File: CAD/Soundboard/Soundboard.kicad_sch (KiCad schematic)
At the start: 23 parts, among them P1 USB_C_Plug_USB2.0, SW1 SW_SPST, SW10 SW_SPST, SW11 SW_SPST, SW12 SW_SPST, SW13 SW_SPST, SW14 SW_SPST, SW15 SW_SPST, SW16 SW_SPST, SW2 SW_SPST, SW3 SW_SPST, SW4 SW_SPST, SW5 SW_SPST, SW6 SW_SPST, SW7 SW_SPST, SW8 SW_SPST, SW9 SW_SPST

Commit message: add a bunch of submodule repos, add some fancy plexing circuits place and route
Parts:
- removed P1: USB_C_Plug_USB2.0, symbol Connector:USB_C_Plug_USB2.0
- added C1: I dont know something big, Capacitor_SMD:C_0805_2012Metric, symbol Device:C
- added J1: USB4085-GF-A_REVB, USB4085-GF-A_REVB:GCT_USB4085-GF-A_REVB, symbol USB4085-GF-A_REVB:USB4085-GF-A_REVB
- added JP1: HEADER-1X876MIL, Connector_PinHeader_2.54mm:PinHeader_1x08_P2.54mm_Vertical, symbol Adafruit USB Type C Downstream Breakout rev B-eagle-import:HEADER-1X876MIL
- added Q1, Q2, Q3, Q4: IRLML6401, Package_TO_SOT_SMD:SOT-23, symbol Transistor_FET:IRLML6401
- added R3, R4: 5.1K, Resistor_SMD:R_0805_2012Metric, symbol Adafruit USB Type C Downstream Breakout rev B-eagle-import:RESISTOR_0603_NOOUT
- added R5, R6, R7, R8: 300, Resistor_SMD:R_0805_2012Metric, symbol Device:R
- added R9: 2.2 K, Resistor_SMD:R_0805_2012Metric, symbol Device:R
- added ST1, ST10, ST11, ST12, ST13, ST14, ST15, ST16, ST2, ST3, ST4, ST5, ST6, ST7, ST8, ST9: ASMB-MTB1-0A3A2, LED_SMD:LED_Avago_PLCC4_3.2x2.8mm_CW, symbol LED:ASMB-MTB1-0A3A2
- added U1: TLC59283DBQ, TLC59283DBQ:DBQ24_TEX, symbol TLC59283DBQ:TLC59283DBQ
- Brd1: footprint (none) -> Display:Adafruit_SSD1306
- D1, D2: footprint (none) -> LED_THT:LED_D5.0mm_Clear
- R1, R2: footprint (none) -> Resistor_THT:R_Axial_DIN0204_L3.6mm_D1.6mm_P7.62mm_Horizontal
- SW1, SW10, SW11, SW12, SW13, SW14, SW15, SW16, SW2, SW3, SW4, SW5, SW6, SW7, SW8, SW9: footprint (none) -> Switch_Keyboard_Cherry_MX:SW_Cherry_MX_PCB_1.00u
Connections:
- net USB_GND is gone; now on net GND: A1.TP1 (USB_GND)
- net GND: now also C1.1, J1.A1 (GND), J1.A12 (GND), J1.B1 (GND), J1.B12 (GND), J1.S1 (SHELL), J1.S2 (SHELL), J1.S3 (SHELL), J1.S4 (SHELL), JP1.1, R3.1, R4.1, R9.1, U1.1 (GND)
- net GPIO0: now also SW4.1 (A); no longer SW1.1 (A)
- net GPIO1: now also SW3.1 (A); no longer SW2.1 (A)
- net GPIO10: now also SW10.1 (A); no longer SW11.1 (A)
- net GPIO11: now also SW9.1 (A); no longer SW12.1 (A)
- net GPIO12: now also SW16.1 (A); no longer SW13.1 (A)
- net GPIO13: now also SW15.1 (A); no longer SW14.1 (A)
- net GPIO14: now also SW14.1 (A); no longer SW15.1 (A)
- net GPIO15: now also SW13.1 (A); no longer SW16.1 (A)
- net GPIO2: now also SW2.1 (A); no longer SW3.1 (A)
- net GPIO22: now also A1.29 (GPIO22)
- net GPIO28: now also A1.34 (GPIO28_ADC2)
- net GPIO3: now also SW1.1 (A); no longer SW4.1 (A)
- net GPIO4: now also SW8.1 (A); no longer SW5.1 (A)
- net GPIO5: now also SW7.1 (A); no longer SW6.1 (A)
- net GPIO6: now also SW6.1 (A); no longer SW7.1 (A)
- net GPIO7: now also SW5.1 (A); no longer SW8.1 (A)
- net GPIO8: now also SW12.1 (A); no longer SW9.1 (A)
- net GPIO9: now also SW11.1 (A); no longer SW10.1 (A)
- net LED LAT: now reaches A1.21 (GPIO16)
- net LED LAT: now also U1.4 (LAT)
- net LED BLANK: now reaches A1.22 (GPIO17)
- net LED BLANK: now also U1.21 (BLANK)
- net LED SIN: now reaches A1.24 (GPIO18)
- net LED SIN: now also U1.2 (SIN)
- net LED SCLK: now reaches A1.25 (GPIO19)
- net LED SCLK: now also U1.3 (SCLK)
- net VBUS: now reaches A1.39 (VSYS)
- net VBUS: now also J1.A4 (VBUS), J1.A9 (VBUS), J1.B4 (VBUS), J1.B9 (VBUS), JP1.2
- net USB_DM renamed D-
- net D-: now also J1.A7 (DN1), J1.B7 (DN2), JP1.5
- net USB_DP renamed D+
- net D+: now also J1.A6 (DP1), J1.B6 (DP2), JP1.6
- net VBUS_5V: no longer names the net of A1.40 (VBUS)
- new net: ST1.1 (RK), ST2.1 (RK), ST3.1 (RK), ST4.1 (RK), U1.9 (OUT4)
- new net: ST1.2 (GK), ST2.2 (GK), ST3.2 (GK), ST4.2 (GK), U1.10 (OUT5)
- new net: ST1.3 (BK), ST2.3 (BK), ST3.3 (BK), ST4.3 (BK), U1.11 (OUT6)
- new net: Q4.3 (D), ST12.4 (A), ST16.4 (A), ST4.4 (A), ST8.4 (A)
- new net: Q2.1 (G), R6.2, U1.6 (OUT1)
- new net: Q1.2 (S), Q2.2 (S), Q3.2 (S), Q4.2 (S), R5.1, R6.1, R7.1, R8.1
- new net: Q2.3 (D), ST10.4 (A), ST14.4 (A), ST2.4 (A), ST6.4 (A)
- new net: ST10.1 (RK), ST11.1 (RK), ST12.1 (RK), ST9.1 (RK), U1.15 (OUT10)
- new net: ST10.2 (GK), ST11.2 (GK), ST12.2 (GK), ST9.2 (GK), U1.16 (OUT11)
- new net: ST10.3 (BK), ST11.3 (BK), ST12.3 (BK), ST9.3 (BK), U1.17 (OUT12)
- new net: Q3.3 (D), ST11.4 (A), ST15.4 (A), ST3.4 (A), ST7.4 (A)
- new net: C1.2, U1.24 (VCC)
- new net: ST13.1 (RK), ST14.1 (RK), ST15.1 (RK), ST16.1 (RK), U1.18 (OUT13)
- new net: ST13.2 (GK), ST14.2 (GK), ST15.2 (GK), ST16.2 (GK), U1.19 (OUT14)
- new net: ST13.3 (BK), ST14.3 (BK), ST15.3 (BK), ST16.3 (BK), U1.20 (OUT15)
- new net: Q3.1 (G), R7.2, U1.7 (OUT2)
- new net: R9.2, U1.23 (IREF)
- new net: ST5.1 (RK), ST6.1 (RK), ST7.1 (RK), ST8.1 (RK), U1.12 (OUT7)
- new net: ST5.2 (GK), ST6.2 (GK), ST7.2 (GK), ST8.2 (GK), U1.13 (OUT8)
- new net: ST5.3 (BK), ST6.3 (BK), ST7.3 (BK), ST8.3 (BK), U1.14 (OUT9)
- new net: Q1.1 (G), R5.2, U1.5 (OUT0)
- new net: Q4.1 (G), R8.2, U1.8 (OUT3)
- new net: Q1.3 (D), ST1.4 (A), ST13.4 (A), ST5.4 (A), ST9.4 (A)
- new net CC1: J1.B5 (CC2), JP1.4, R4.2
- new net CC2: J1.A5 (CC1), JP1.8, R3.2
- new net SBU1: J1.A8 (SBU1), JP1.7
- new net SBU2: J1.B8 (SBU2), JP1.3
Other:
- note added: "Please note, the TLC59283DBQ's referance current should be set to aprox. 25mA with a 2.2K resistor with 25mA the P channel transistor the minimium value of the pull up resitor is given by r_min = enabled_voltage / sink_current from this we get the min R is 180 Some testing may review a better higher value. I think we will start with 300"
- note added: "Set to UFP (Peripheral) Also marks this as a USB 2.0 peripheral device For DFP (Host) you need pullups here instead of pulldowns."
- note added: "Upstream/Downstream Facing Port Setup:"
- moved on the sheet: Brd1, D1, D2, R1, R2

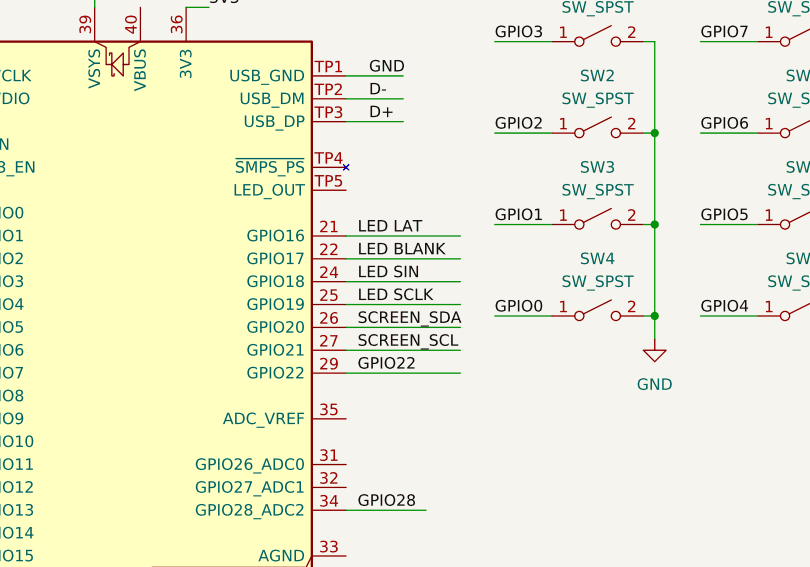
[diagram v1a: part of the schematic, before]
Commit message: swap led sclk and sin
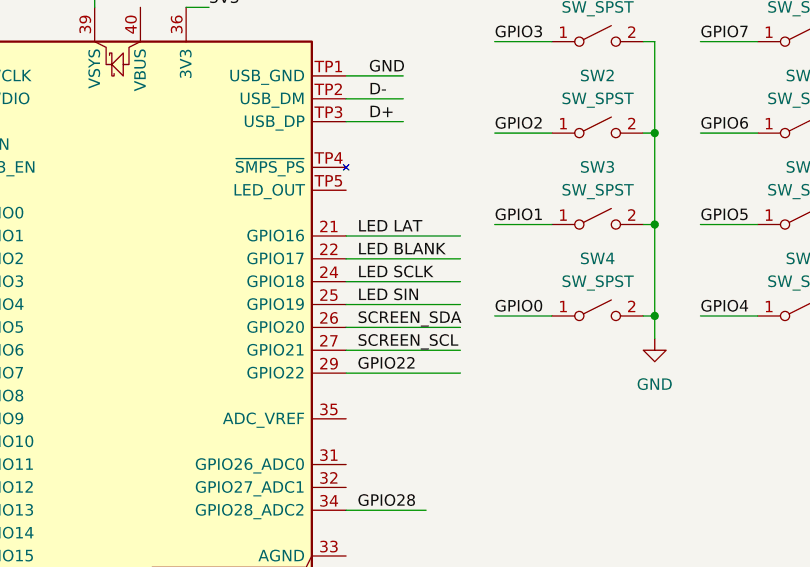
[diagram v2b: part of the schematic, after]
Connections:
- net LED SCLK: now also A1.24 (GPIO18); no longer A1.25 (GPIO19)
- net LED SIN: now also A1.25 (GPIO19); no longer A1.24 (GPIO18)
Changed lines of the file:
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@@
+		)
+	)
+	(label "LED SIN"
+		(at 116.84 57.15 0)
+		(effects
+			(font
+				(size 1.27 1.27)
+			)
+			(justify left bottom)
 		)
 	)
@@
 	)
 	(label "LED SCLK"
-		(at 116.84 57.15 0)
-		(effects
-			(font
-				(size 1.27 1.27)
-			)
-			(justify left bottom)
-		)
-	)
-	(label "LED SCLK"
 		(at 134.62 257.81 0)
 		(effects
@@
 		)
 	)
+	(label "LED SCLK"
+		(at 116.84 54.61 0)
+		(effects
+			(font
+				(size 1.27 1.27)
+			)
+			(justify left bottom)
+		)
+	)
 	(label "CC2"
 		(at 54.61 130.81 0)
@@
 		(effects
 			(font
-				(size 1.27 1.27)
-			)
-			(justify left bottom)
-		)
-	)
-	(label "LED SIN"
-		(at 116.84 54.61 0)
-		(effects
-			(font

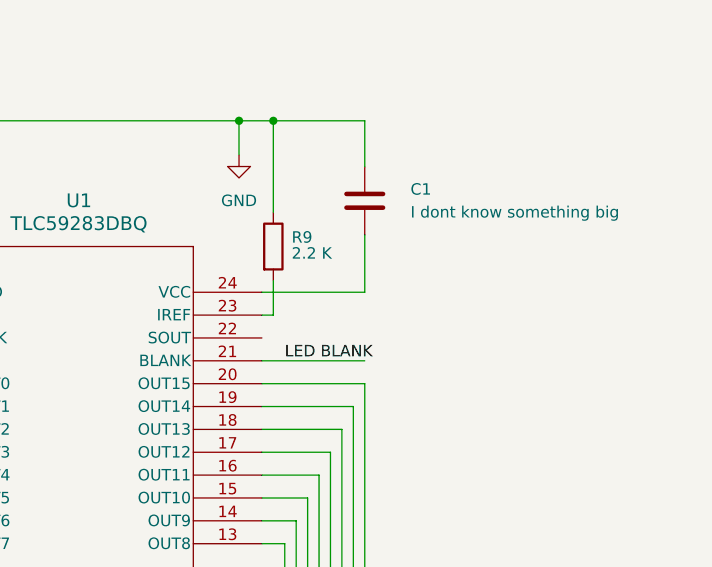
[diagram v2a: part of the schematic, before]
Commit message: move some caps
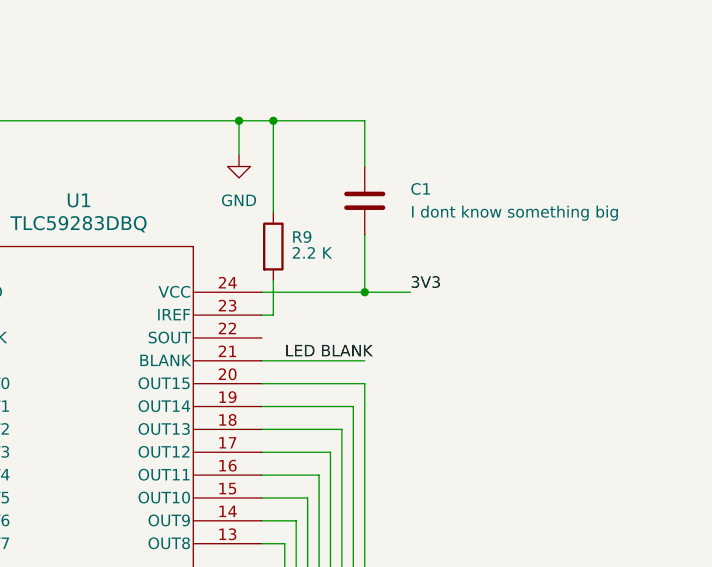
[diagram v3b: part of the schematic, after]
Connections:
- net 3V3: now also C1.2, U1.24 (VCC)
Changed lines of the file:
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@@
 	)
 	(junction
+		(at 189.23 280.67)
+		(diameter 0)
+		(color 0 0 0 0)
+	)
+	(junction
 		(at 19.05 39.37)
 		(diameter 0)
@@
 	(wire
 		(pts
+			(xy 189.23 280.67) (xy 194.31 280.67)
+		)
+		(stroke
+			(width 0)
+			(type default)
+		)
+	)
+	(wire
+		(pts
 			(xy 72.39 283.21) (xy 72.39 294.64)
 		)
@@
 		(effects
 			(font
+				(size 1.27 1.27)
+			)
+			(justify left bottom)
+		)
+	)
+	(label "3V3"
+		(at 194.31 280.67 0)
+		(effects
+			(font
